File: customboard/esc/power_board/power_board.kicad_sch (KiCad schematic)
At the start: 27 parts, among them J1 Conn_01x08_MountingPin, J2 Conn_01x01, J3 Conn_01x01, U2 AP7381-50SA-7, U3 AP7381-33SA-7, U4 AP7381-50SA-7, U5 AP7381-50SA-7, U6 AP7381-50SA-7, U7 AP7381-33SA-7

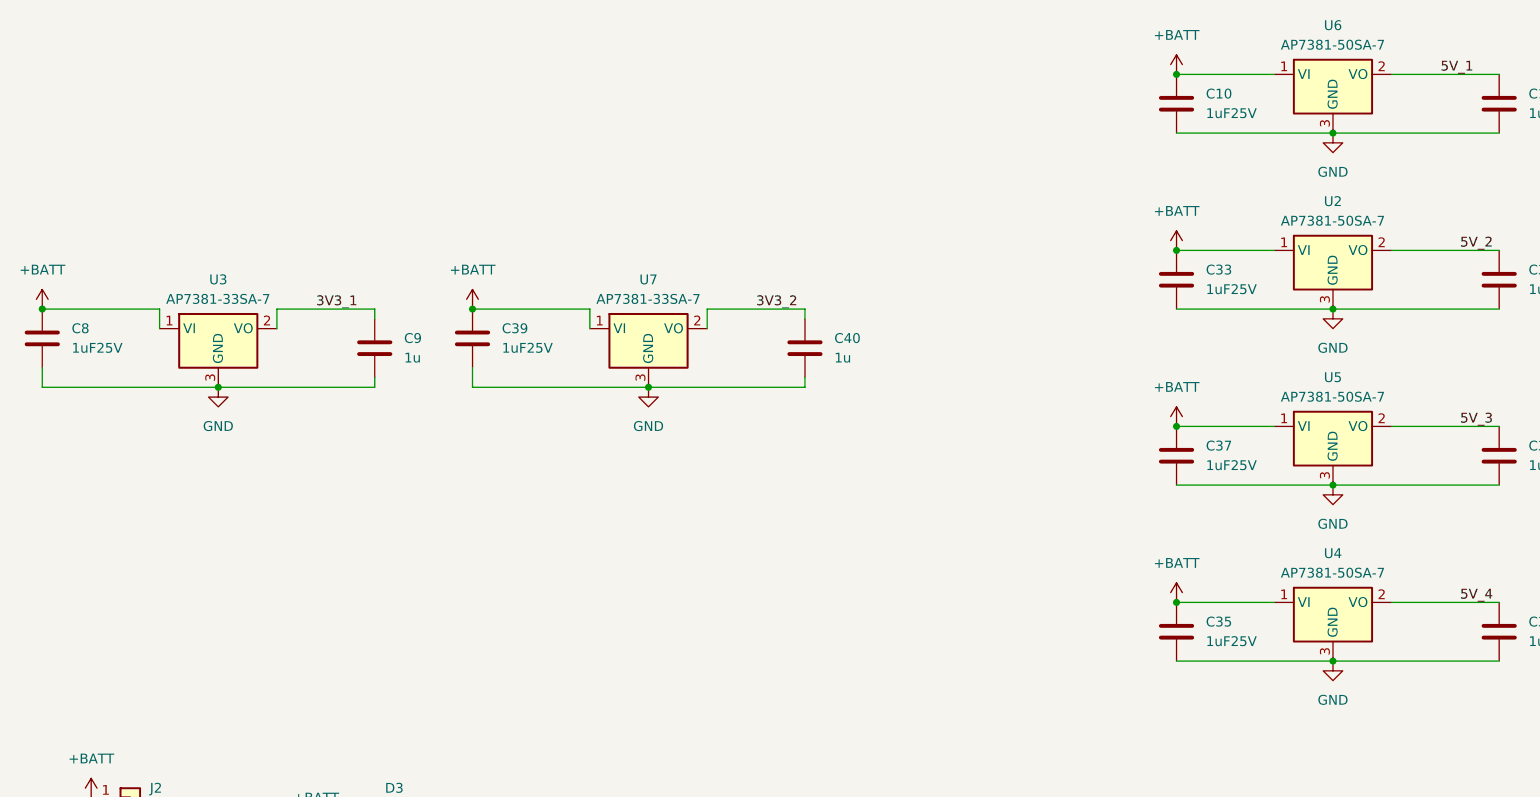
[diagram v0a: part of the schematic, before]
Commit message: sot-89 regulator
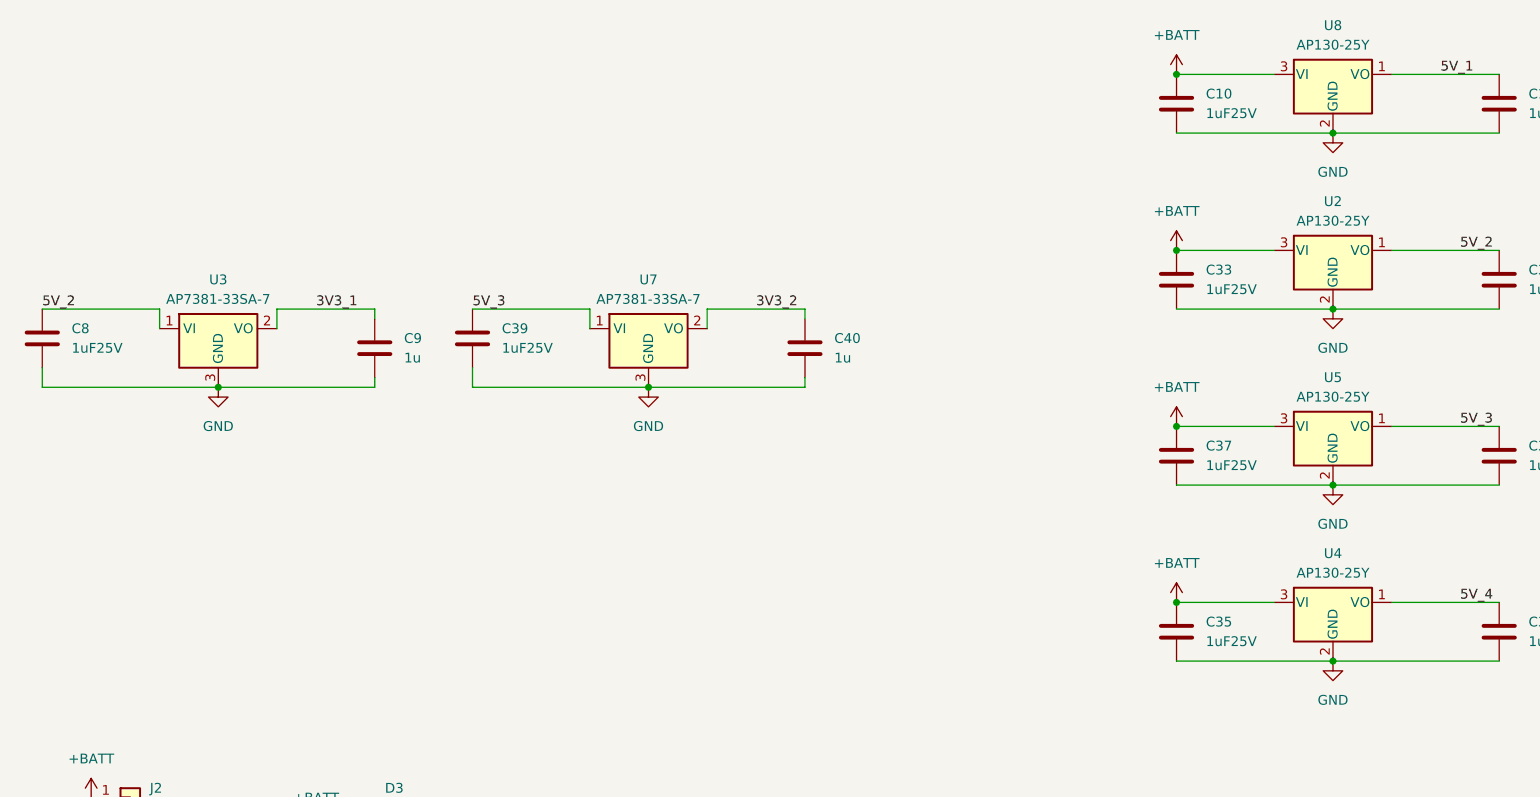
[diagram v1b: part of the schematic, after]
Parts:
- removed U2, U4, U5, U6: AP7381-50SA-7, Package_TO_SOT_SMD:SOT-23, symbol Regulator_Linear:AP7381-50SA-7
- added U2, U4, U5, U8: AP130-25Y, Package_TO_SOT_SMD:SOT-89-3, symbol Regulator_Linear:AP130-25Y
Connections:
- net +BATT: now also U2.3 (VI), U4.3 (VI), U5.3 (VI), U8.3 (VI); no longer C39.1, C8.1, U3.1 (VI), U7.1 (VI)
- net 5V_1: now also U8.1 (VO)
- net 5V_2: now also C8.1, U3.1 (VI), U2.1 (VO)
- net 5V_3: now also C39.1, U7.1 (VI), U5.1 (VO)
- net 5V_4: now also U4.1 (VO)
- net GND: now also U2.2 (GND), U4.2 (GND), U5.2 (GND), U8.2 (GND)

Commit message: narrower castelations on logic board; proper stls
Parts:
- J2, J3, U1: now left out of the parts list
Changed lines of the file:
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@@
 		(unit 1)
 		(exclude_from_sim no)
-		(in_bom yes)
+		(in_bom no)
 		(on_board yes)
 		(dnp no)
@@
 		(unit 1)
 		(exclude_from_sim no)
-		(in_bom yes)
+		(in_bom no)
 		(on_board yes)
 		(dnp no)
@@
 		(unit 1)
 		(exclude_from_sim no)
-		(in_bom yes)
-		(on_board yes)
-		(dnp no)
+		(in_bom no)
+		(on_board yes)
+		(dnp no)
